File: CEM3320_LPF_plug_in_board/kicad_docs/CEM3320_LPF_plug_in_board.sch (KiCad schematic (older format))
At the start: 42 parts, among them J1 signal_in, J2 signal_in, J3 signal_out, J4 Conn_01x08_Male, U1 CEM3320, U2 TL072

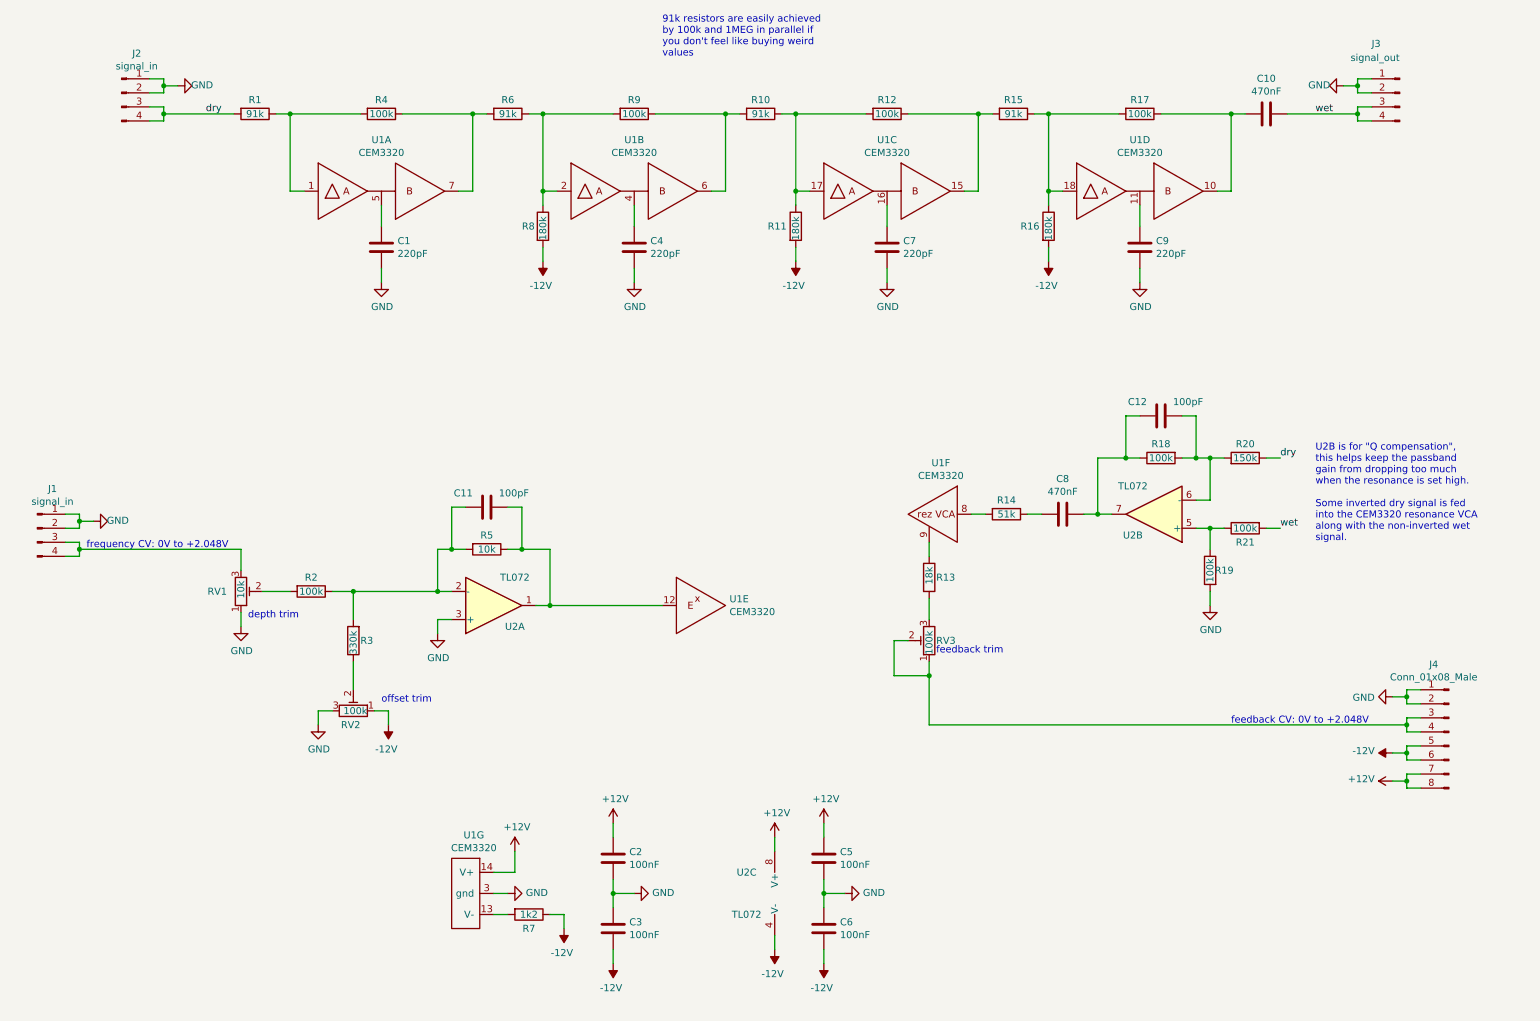
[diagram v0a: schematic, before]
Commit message: clean up CEM3320 LPF, add smd cap footprints for timing caps
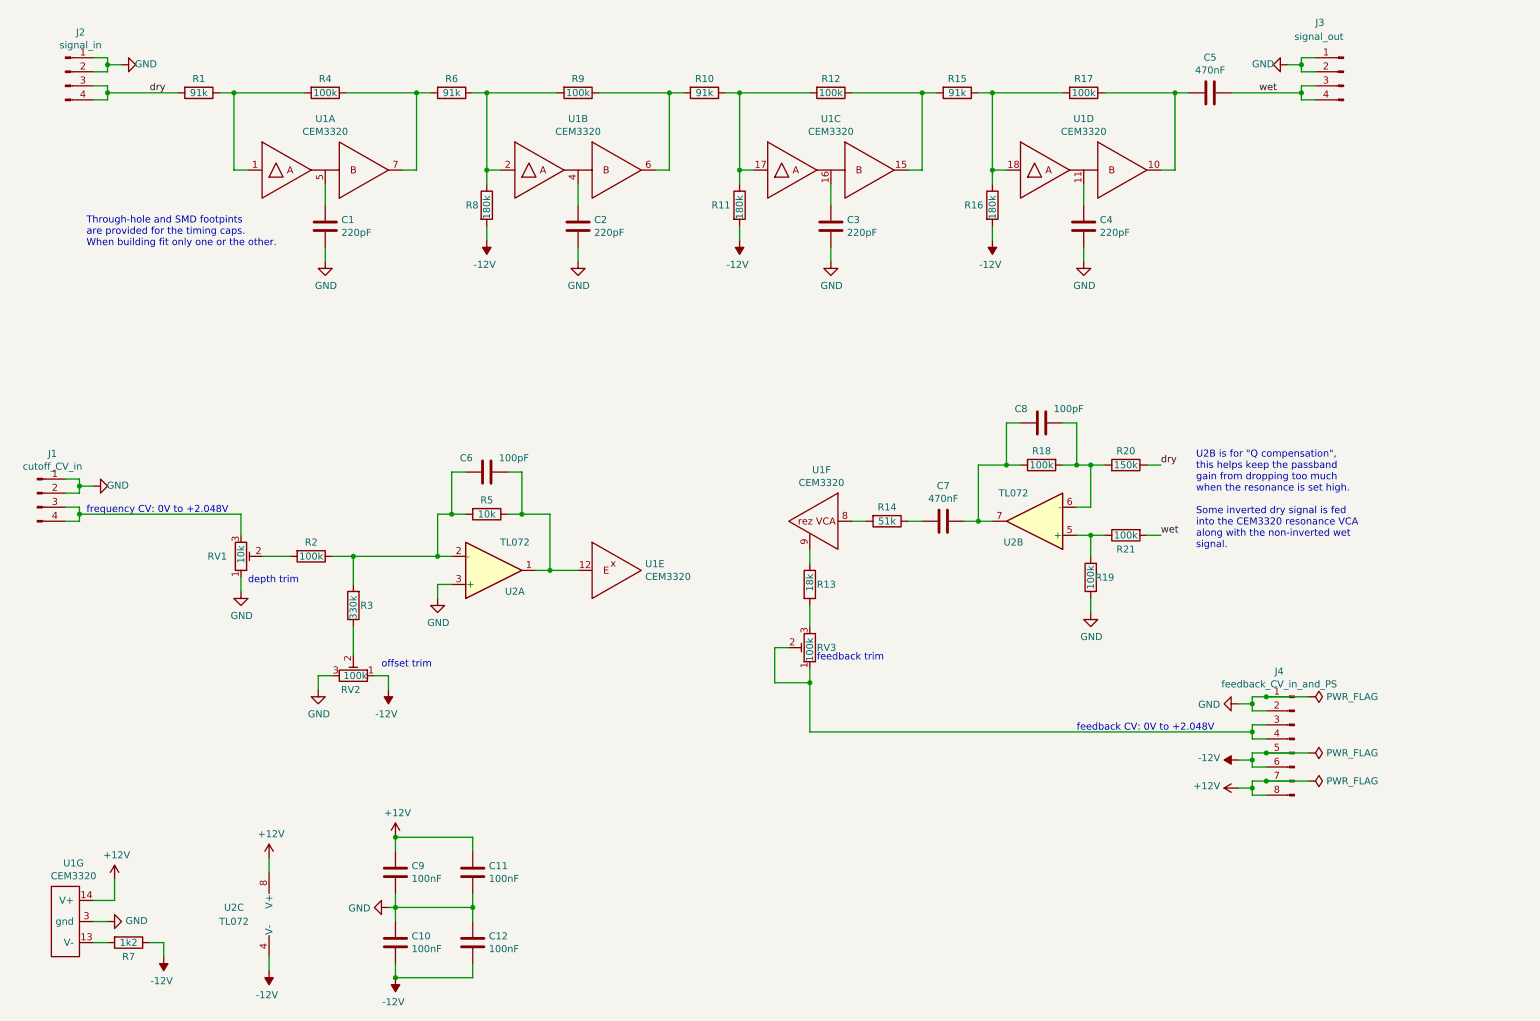
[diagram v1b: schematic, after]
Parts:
- removed C7, C9: 220pF, Capacitor_THT:C_Rect_L7.0mm_W4.5mm_P5.00mm, symbol Device:C
- added C2, C3: 220pF, cem3320:timing_cap_dual_fp, symbol Device:C
- C1, C4: footprint Capacitor_THT:C_Rect_L7.0mm_W4.5mm_P5.00mm -> cem3320:timing_cap_dual_fp
- J1: value signal_in -> cutoff_CV_in
- J4: value Conn_01x08_Male -> feedback_CV_in_and_PS
- RV1, RV2, RV3: footprint Potentiometer_SMD:Potentiometer_Bourns_3269W_Vertical -> Potentiometer_THT:Potentiometer_Bourns_3296W_Vertical
- renumbered C3 to C10, C5 to C11, C6 to C12, C10 to C5, C11 to C6, C8 to C7, C12 to C8, C2 to C9
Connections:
- net GND: now also C2.2, C3.2
- net at U1.4: now also C2.1; no longer C4.1
- net at U1.16: now also C3.1
- net at U1.11: now also C4.1
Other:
- note added: "Through-hole and SMD footpints\nare provided for the timing caps.\nWhen building fit only one or the other."
- note removed: "91k resistors are easily achieved \nby 100k and 1MEG in parallel if\nyou don't feel like buying weird \nvalues"
- moved on the sheet: C1, C10, C11, C12, C5, C6, C7, C8, C9, J1, J2, J3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

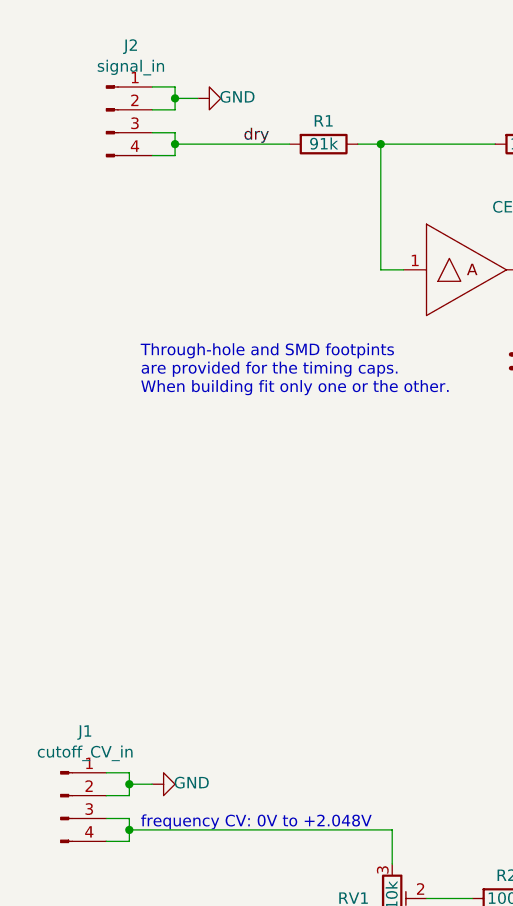
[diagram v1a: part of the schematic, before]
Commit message: swap j2 and j1 positions for consistency
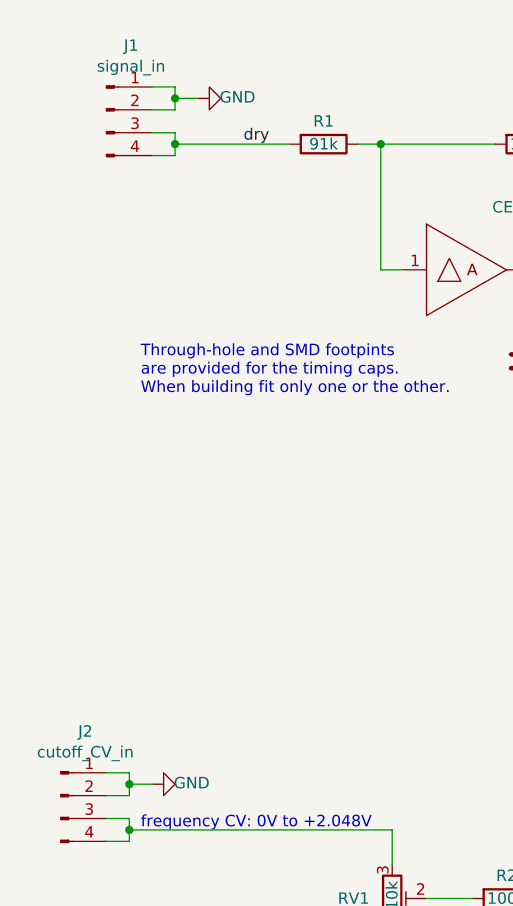
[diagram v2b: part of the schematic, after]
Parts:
- renumbered J2 to J1, J1 to J2
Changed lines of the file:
@@
 Connection ~ 7000 1200
 $Comp
-L Connector:Conn_01x04_Male J2
+L Connector:Conn_01x04_Male J1
 U 1 1 5D018601
 P 900 1050
-F 0 "J2" H 1008 1331 50  0000 C CNN
+F 0 "J1" H 1008 1331 50  0000 C CNN
 F 1 "signal_in" H 1008 1240 50  0000 C CNN
 F 2 "Connector_PinHeader_2.54mm:PinHeader_1x04_P2.54mm_Vertical" H 900 1050 50  0001 C CNN
@@
 	9350 6150 9350 6200
 $Comp
-L Connector:Conn_01x04_Male J1
+L Connector:Conn_01x04_Male J2
 U 1 1 5D1784CF
 P 700 4050
-F 0 "J1" H 808 4331 50  0000 C CNN
+F 0 "J2" H 808 4331 50  0000 C CNN
 F 1 "cutoff_CV_in" H 808 4240 50  0000 C CNN
 F 2 "Connector_PinHeader_2.54mm:PinHeader_1x04_P2.54mm_Vertical" H 700 4050 50  0001 C CNN
